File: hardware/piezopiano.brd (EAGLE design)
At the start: 90 x 99.8 mm, 110 parts, among them J2 CON2, Q1 DMN3404L, Q2 DMN3404L, Q3 DMN3404L, Q4 DMN3404L, Q5 DMN3404L, Q6 DMN3404L, Q7 DMN3404L, Q8 DMN3404L, Q9 DNP, U1 CH340E_MSOP10, U2 ATMEGA4809, U3 DNP

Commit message: Reverted to local libraries
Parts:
- DEBUG: value AVR-UPDI-6-SKEDD -> DNP
- JP1, JP2, JP3, JP4, JP5, JP6: value PINROW-1X5 -> DNP

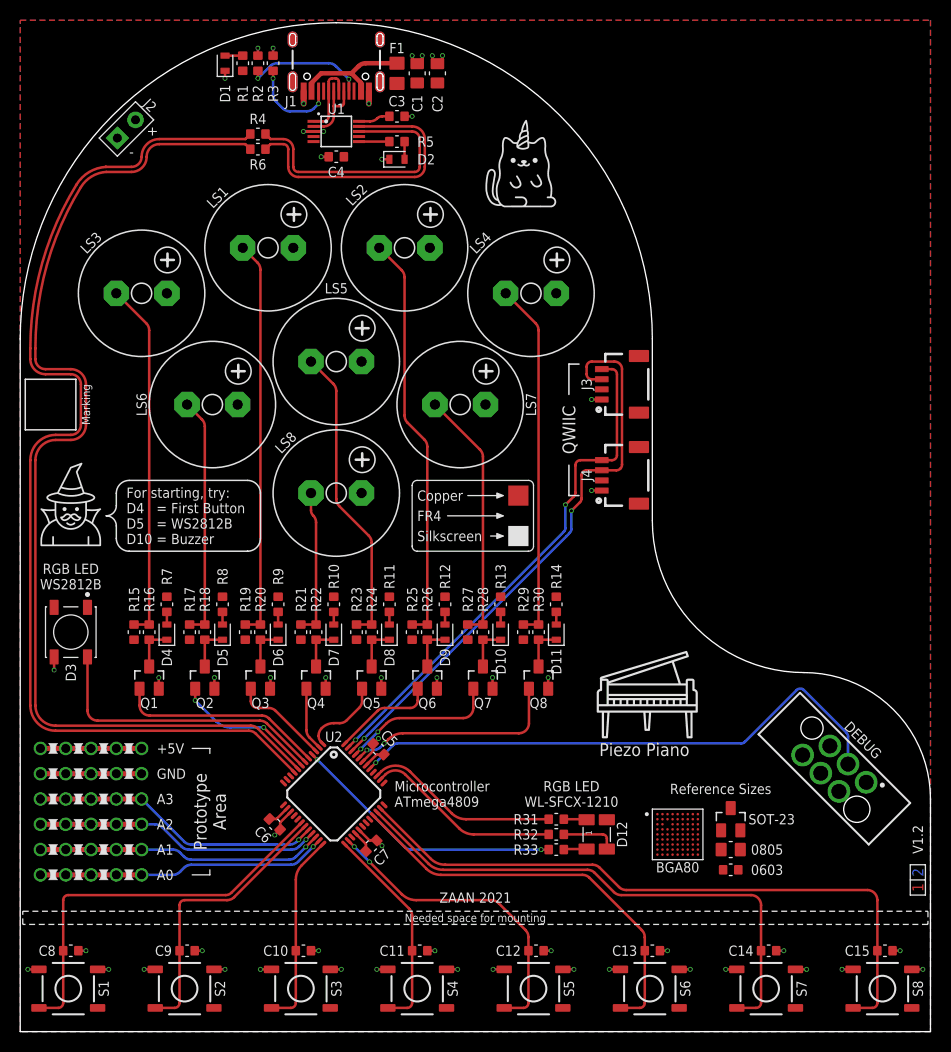
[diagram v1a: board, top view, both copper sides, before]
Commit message: Fixed silkscreen errors
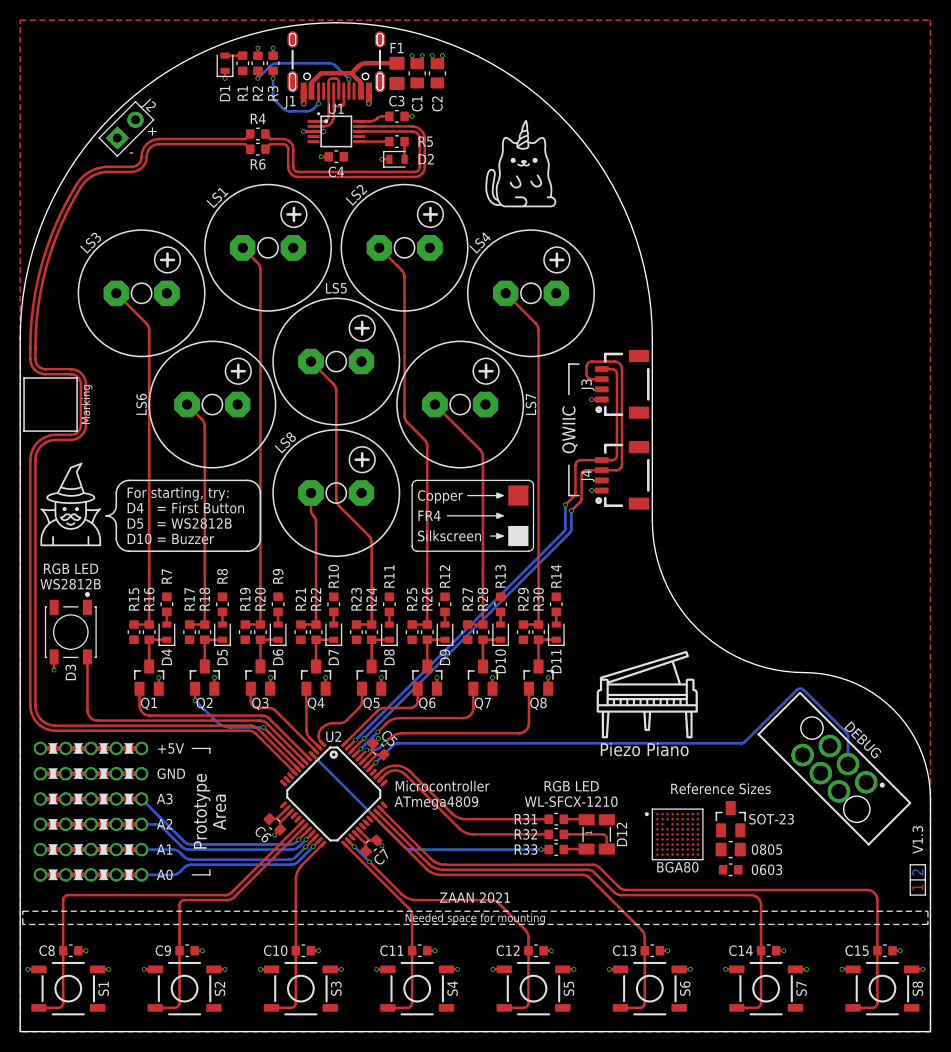
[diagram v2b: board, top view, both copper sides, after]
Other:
- board text added: "V1.3"
- board text removed: "V1.2"
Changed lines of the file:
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@@
 <drawing>
 <settings>
-<setting alwaysvectorfont="no"/>
+<setting alwaysvectorfont="yes"/>
 <setting verticaltext="up"/>
 </settings>
@@
 <layer number="24" name="bOrigins" color="15" fill="1" visible="yes" active="yes"/>
 <layer number="25" name="tNames" color="7" fill="1" visible="yes" active="yes"/>
-<layer number="26" name="bNames" color="7" fill="1" visible="no" active="yes"/>
+<layer number="26" name="bNames" color="7" fill="1" visible="yes" active="yes"/>
 <layer number="27" name="tValues" color="7" fill="1" visible="no" active="yes"/>
 <layer number="28" name="bValues" color="7" fill="1" visible="no" active="yes"/>
@@
 ornare magna eget, malesuada nunc. Fusce malesuada massa felis, cursus finibus dui
 viverra ut. Duis commodo finibus commodo. Morbi sodales vulputate mauris, eget
-molestie ex gravida quis. Phasellus tempus velit eu orci lacinia imperdiet. Proin eget
-ipsum non lectus mattis mollis vitae id arcu. Curabitur semper tempus dignissim. Nunc
+molestie ex gravida quis. Phasellus  tempus velit eu orci lacinia imperdiet. Proin eget
+ipsum non lectus mattis mollis vitae   arcu. Curabitur semper tempus dignissim. Nunc
 efficitur magna vel nisi maximus, rhoncus laoreet leo vestibulum. Proin maximus convallis
 est ut eleifend. Etiam sollicitudin sem id congue rutrum. Integer suscipit, ante in
 consequat condimentum, est erat tempus purus, sed fringilla tortor augue sed justo.
 Ut non nisl sit amet arcu cursus commodo eget et metus.</text>
-<text x="88.75" y="19" size="1.016" layer="21" font="vector" ratio="15" rot="R90" align="center">V1.2</text>
+<text x="88.75" y="19" size="1.016" layer="21" font="vector" ratio="15" rot="R90" align="center">V1.3</text>
 <text x="57.25" y="27.25" size="1.27" layer="21" font="vector" ratio="15">Piezo Piano</text>
 <text x="10.5" y="51" size="1.016" layer="21" font="vector" ratio="15" align="center-left">For starting, try:
@@
 <via x="56.5" y="53.5" extent="1-16" drill="0.3"/>
 <contactref element="J2" pad="1"/>
-<wire x1="39.75" y1="96.5" x2="40.75" y2="96.5" width="0" layer="19" extent="1-1"/>
-<wire x1="35.57" y1="98.095" x2="38.75" y2="96.5" width="0" layer="19" extent="16-16"/>
 <wire x1="35.57" y1="98.095" x2="35.57" y2="98.095" width="0" layer="19" extent="1-16"/>
-<wire x1="35.57" y1="93.915" x2="39.25" y2="95.7" width="0" layer="19" extent="1-16"/>
 <wire x1="35.57" y1="93.915" x2="35.57" y2="93.915" width="0" layer="19" extent="1-16"/>
-<wire x1="34.475" y1="92.99" x2="35.57" y2="93.915" width="0" layer="19" extent="1-16"/>
-<wire x1="38" y1="90.5" x2="34.475" y2="91.75" width="0" layer="19" extent="1-1"/>
-<wire x1="36.5" y1="86.25" x2="38" y2="90.5" width="0" layer="19" extent="1-1"/>
-<wire x1="30" y1="89" x2="34.475" y2="91.75" width="0" layer="19" extent="1-1"/>
-<wire x1="29.75" y1="86.5" x2="30" y2="89" width="0" layer="19" extent="1-1"/>
-<wire x1="28.025" y1="91.75" x2="28" y2="89" width="0" layer="19" extent="1-1"/>
-<wire x1="26.93" y1="93.915" x2="28.025" y2="92.99" width="0" layer="19" extent="1-16"/>
+<wire x1="26.93" y1="98.095" x2="26.93" y2="98.095" width="0" layer="19" extent="1-16"/>
 <wire x1="26.93" y1="93.915" x2="26.93" y2="93.915" width="0" layer="19" extent="1-16"/>
-<wire x1="25" y1="96.5" x2="26.93" y2="93.915" width="0" layer="19" extent="1-16"/>
-<wire x1="23.5" y1="97.25" x2="25" y2="97.25" width="0" layer="19" extent="1-1"/>
-<wire x1="26.93" y1="98.095" x2="25" y2="97.25" width="0" layer="19" extent="16-16"/>
-<wire x1="26.93" y1="98.095" x2="26.93" y2="98.095" width="0" layer="19" extent="1-16"/>
-<wire x1="20.25" y1="95" x2="23.5" y2="96.5" width="0" layer="19" extent="1-1"/>
-<wire x1="9.601971875" y1="88.351971875" x2="20.25" y2="94.25" width="0" layer="19" extent="1-1"/>
-<wire x1="56.5" y1="62.5" x2="36.5" y2="86.25" width="0" layer="19" extent="1-1"/>
-<wire x1="57.5" y1="53.5" x2="57.5" y2="62.5" width="0" layer="19" extent="1-1"/>
-<wire x1="52.2" y1="35" x2="56.5" y2="53.5" width="0" layer="19" extent="1-1"/>
-<wire x1="46.7" y1="33.9" x2="52.2" y2="33.9" width="0" layer="19" extent="1-1"/>
-<wire x1="41.2" y1="33.9" x2="46.7" y2="33.9" width="0" layer="19" extent="1-1"/>
-<wire x1="35.7" y1="33.9" x2="41.2" y2="33.9" width="0" layer="19" extent="1-1"/>
-<wire x1="35.419415625" y1="28.980075" x2="35.7" y2="33.9" width="0" layer="19" extent="1-1"/>
-<wire x1="30.2" y1="33.9" x2="35.7" y2="33.9" width="0" layer="19" extent="1-1"/>
-<wire x1="24.75" y1="35" x2="30.2" y2="35" width="0" layer="19" extent="1-1"/>
-<wire x1="19.2" y1="33.9" x2="24.7" y2="33.9" width="0" layer="19" extent="1-1"/>
-<wire x1="13.7" y1="33.9" x2="19.2" y2="33.9" width="0" layer="19" extent="1-1"/>
-<wire x1="33.49255" y1="19.9467875" x2="33.846103125" y2="26.69965625" width="0" layer="19" extent="1-1"/>
-<wire x1="26.73968125" y1="21.714553125" x2="33.49255" y2="19.9467875" width="0" layer="19" extent="1-1"/>
-<wire x1="12" y1="25.5" x2="13.7" y2="33.9" width="0" layer="19" extent="1-1"/>
-<wire x1="9.5" y1="25.5" x2="12" y2="25.5" width="0" layer="19" extent="1-1"/>
-<wire x1="7" y1="25.5" x2="9.5" y2="25.5" width="0" layer="19" extent="1-1"/>
-<wire x1="4.5" y1="25.5" x2="7" y2="25.5" width="0" layer="19" extent="1-1"/>
-<wire x1="2" y1="25.5" x2="4.5" y2="25.5" width="0" layer="19" extent="1-1"/>
-<wire x1="3.35" y1="35.75" x2="4.5" y2="25.5" width="0" layer="19" extent="1-1"/>
-<wire x1="40.25" y1="8" x2="35.77296875" y2="18.373475" width="0" layer="19" extent="1-1"/>
-<wire x1="42.15" y1="6.155" x2="41" y2="8" width="0" layer="19" extent="1-1"/>
-<wire x1="46.75" y1="6.155" x2="43.25" y2="6.155" width="0" layer="19" extent="1-1"/>
-<wire x1="51.75" y1="8" x2="47.85" y2="6.155" width="0" layer="19" extent="1-1"/>
-<wire x1="53.65" y1="6.155" x2="52.5" y2="8" width="0" layer="19" extent="1-1"/>
-<wire x1="58.25" y1="6.155" x2="54.75" y2="6.155" width="0" layer="19" extent="1-1"/>
-<wire x1="63.25" y1="8" x2="59.35" y2="6.155" width="0" layer="19" extent="1-1"/>
-<wire x1="65.15" y1="6.155" x2="64" y2="8" width="0" layer="19" extent="1-1"/>
-<wire x1="69.75" y1="6.155" x2="66.25" y2="6.155" width="0" layer="19" extent="1-1"/>
-<wire x1="74.75" y1="8" x2="70.85" y2="6.155" width="0" layer="19" extent="1-1"/>
-<wire x1="76.65" y1="6.155" x2="75.5" y2="8" width="0" layer="19" extent="1-1"/>
-<wire x1="81.25" y1="6.155" x2="77.75" y2="6.155" width="0" layer="19" extent="1-1"/>
-<wire x1="86.25" y1="8" x2="82.35" y2="6.155" width="0" layer="19" extent="1-1"/>
-<wire x1="88.15" y1="6.155" x2="87" y2="8" width="0" layer="19" extent="1-1"/>
-<wire x1="36.35" y1="6.155" x2="40.25" y2="8" width="0" layer="19" extent="1-1"/>
-<wire x1="31.75" y1="6.155" x2="35.25" y2="6.155" width="0" layer="19" extent="1-1"/>
-<wire x1="29.5" y1="8" x2="30.65" y2="6.155" width="0" layer="19" extent="1-1"/>
-<wire x1="24.85" y1="6.155" x2="28.75" y2="8" width="0" layer="19" extent="1-1"/>
-<wire x1="20.25" y1="6.155" x2="23.75" y2="6.155" width="0" layer="19" extent="1-1"/>
-<wire x1="18" y1="8" x2="19.15" y2="6.155" width="0" layer="19" extent="1-1"/>
-<wire x1="13.35" y1="6.155" x2="17.25" y2="8" width="0" layer="19" extent="1-1"/>
-<wire x1="8.75" y1="6.155" x2="12.25" y2="6.155" width="0" layer="19" extent="1-1"/>
-<wire x1="6.5" y1="8" x2="7.65" y2="6.155" width="0" layer="19" extent="1-1"/>
-<wire x1="1.85" y1="6.155" x2="5.75" y2="8" width="0" layer="19" extent="1-1"/>
-<wire x1="80.9490125" y1="23.754934375" x2="86.25" y2="8" width="0" layer="19" extent="1-1"/>
 </signal>
 <signal name="D2">

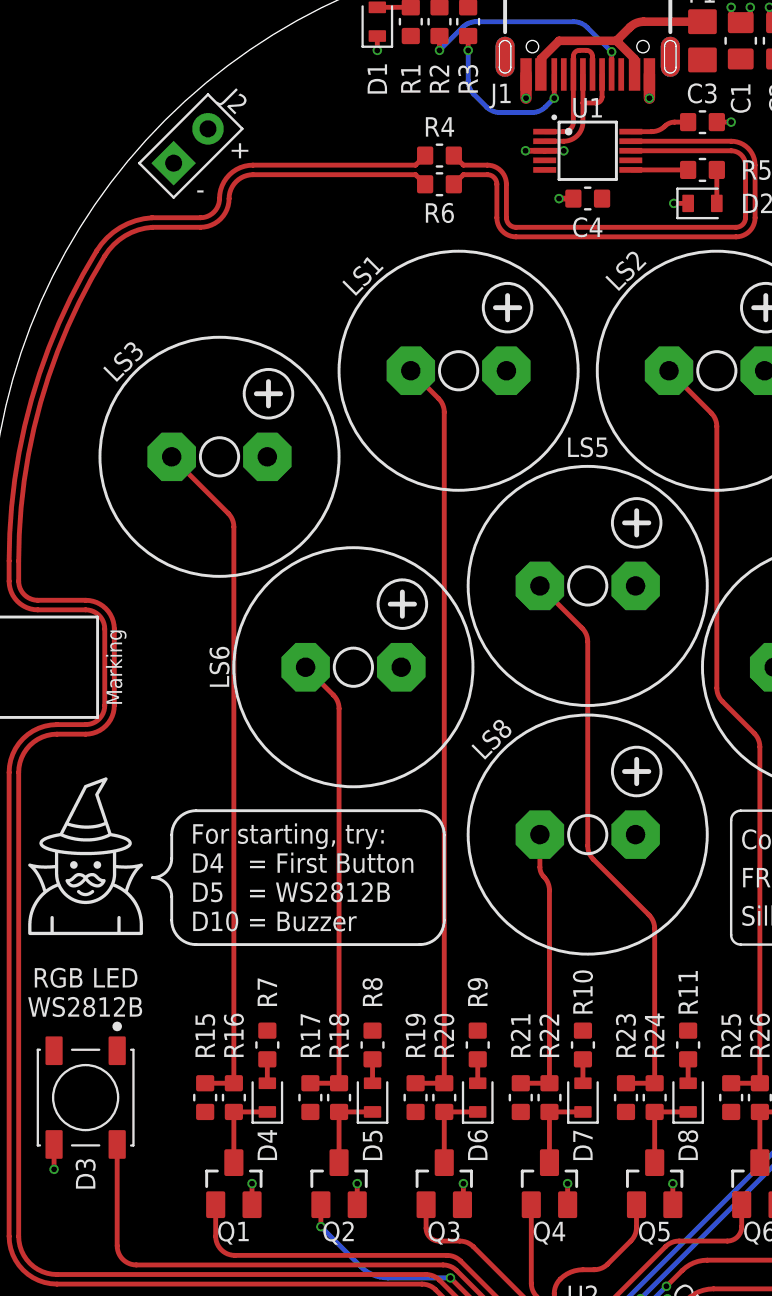
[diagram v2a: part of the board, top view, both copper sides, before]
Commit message: Added UART RST
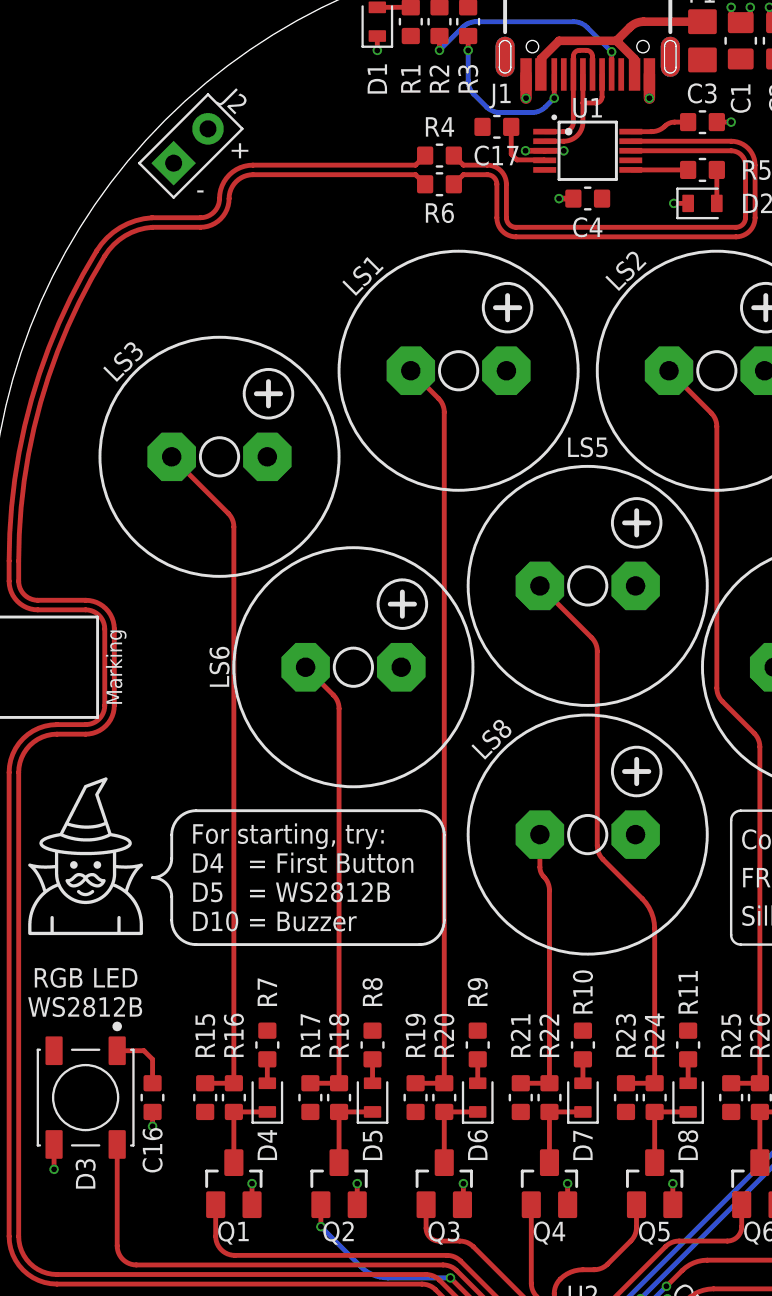
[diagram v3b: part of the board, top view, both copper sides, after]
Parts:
- added C16, C17: 100n, zaan-Capacitors:C0603
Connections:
- new net N$1: C17.1, U1.4
- net +5V: now also C16.1
- net GND: now also C16.2
- net RESETN: now also C17.2
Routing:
- net N$1: track 0.00 -> 3.31 mm
- net +5V: track 6.55 -> 9.83 mm
- net GND: track 57.8 -> 58.6 mm, vias 52 -> 53
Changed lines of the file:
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@@
 <layer number="24" name="bOrigins" color="15" fill="1" visible="yes" active="yes"/>
 <layer number="25" name="tNames" color="7" fill="1" visible="yes" active="yes"/>
-<layer number="26" name="bNames" color="7" fill="1" visible="yes" active="yes"/>
+<layer number="26" name="bNames" color="7" fill="1" visible="no" active="yes"/>
 <layer number="27" name="tValues" color="7" fill="1" visible="no" active="yes"/>
 <layer number="28" name="bValues" color="7" fill="1" visible="no" active="yes"/>
@@
 <element name="U$1" library="zaan-Symbol-Artwork" package="CATICORN-7MM" value="" x="46" y="81.5" smashed="yes"/>
 <element name="U$8" library="zaan-Symbol-Artwork" package="EXPLANATION-2-2MM" package3d_urn="urn:adsk.eagle:package:31668745/2" value="" x="49.25" y="51" smashed="yes" rot="R180"/>
+<element name="C16" library="zaan-Capacitors" package="C0603" package3d_urn="urn:adsk.eagle:package:16758953/4" value="100n" x="8.5" y="39.5" smashed="yes" rot="R270">
+<attribute name="DESCRIPTION" value="Chip Capacitor" x="8.5" y="39.5" size="1.778" layer="27" rot="R270" display="off"/>
+<attribute name="DIELECTRIC" value="X7R" x="8.5" y="39.5" size="1.778" layer="27" rot="R270" display="off"/>
+<attribute name="MF" value="Yageo" x="8.5" y="39.5" size="1.778" layer="27" rot="R270" display="off"/>
+<attribute name="MPN" value="CC0603JRX7R9BB104" x="8.5" y="39.5" size="1.778" layer="27" rot="R270" display="off"/>
+<attribute name="NAME" x="8.5" y="36.75" size="1.016" layer="25" font="vector" ratio="15" rot="R270" align="center"/>
+<attribute name="PACKAGE" value="1606" x="8.5" y="39.5" size="1.778" layer="27" rot="R270" display="off"/>
+<attribute name="PACKAGE-IN" value="0603" x="8.5" y="39.5" size="1.778" layer="27" rot="R270" display="off"/>
+<attribute name="TOLERANCE" value="5%" x="8.5" y="39.5" size="1.778" layer="27" rot="R270" display="off"/>
+<attribute name="VALUE" x="7" y="39.5" size="1.016" layer="27" font="vector" ratio="15" rot="R270" align="center"/>
+<attribute name="VOLTAGE" value="50V" x="8.5" y="39.5" size="1.778" layer="27" rot="R270" display="off"/>
+</element>
+<element name="C17" library="zaan-Capacitors" package="C0603" package3d_urn="urn:adsk.eagle:package:16758953/4" value="100n" x="26.5" y="90.25" smashed="yes" rot="R180">
+<attribute name="DESCRIPTION" value="Chip Capacitor" x="26.5" y="90.25" size="1.778" layer="27" font="vector" ratio="15" rot="R180" display="off"/>
+<attribute name="DIELECTRIC" value="X7R" x="26.5" y="90.25" size="1.778" layer="27" font="vector" ratio="15" rot="R180" display="off"/>
+<attribute name="MF" value="Yageo" x="26.5" y="90.25" size="1.778" layer="27" font="vector" ratio="15" rot="R180" display="off"/>
+<attribute name="MPN" value="CC0603JRX7R9BB104" x="26.5" y="90.25" size="1.778" layer="27" font="vector" ratio="15" rot="R180" display="off"/>
+<attribute name="NAME" x="26.5" y="88.75" size="1.016" layer="25" font="vector" ratio="15" rot="R180" align="center"/>
+<attribute name="PACKAGE" value="1606" x="26.5" y="90.25" size="1.778" layer="27" font="vector" ratio="15" rot="R180" display="off"/>
+<attribute name="PACKAGE-IN" value="0603" x="26.5" y="90.25" size="1.778" layer="27" font="vector" ratio="15" rot="R180" display="off"/>
+<attribute name="TOLERANCE" value="5%" x="26.5" y="90.25" size="1.778" layer="27" font="vector" ratio="15" rot="R180" display="off"/>
+<attribute name="VALUE" x="26.5" y="91.75" size="1.016" layer="27" font="vector" ratio="15" rot="R180" align="center"/>
+<attribute name="VOLTAGE" value="50V" x="26.5" y="90.25" size="1.778" layer="27" font="vector" ratio="15" rot="R180" display="off"/>
+</element>
 </elements>
 <signals>
@@
 <via x="56.5" y="53.5" extent="1-16" drill="0.3"/>
 <contactref element="J2" pad="1"/>
+<contactref element="C16" pad="2"/>
+<wire x1="8.5" y1="38.75" x2="8.5" y2="38" width="0.254" layer="1"/>
+<via x="8.5" y="38" extent="1-16" drill="0.3"/>
 <wire x1="35.57" y1="98.095" x2="35.57" y2="98.095" width="0" layer="19" extent="1-16"/>
 <wire x1="35.57" y1="93.915" x2="35.57" y2="93.915" width="0" layer="19" extent="1-16"/>
@@
 <contactref element="D12" pad="4"/>
 <contactref element="J2" pad="2"/>
+<contactref element="C16" pad="1"/>
+<wire x1="6.65" y1="41.95" x2="8.05" y2="41.95" width="0.254" layer="1"/>
+<wire x1="8.05" y1="41.95" x2="8.5" y2="41.5" width="0.254" layer="1"/>
+<wire x1="8.5" y1="41.5" x2="8.5" y2="40.25" width="0.254" layer="1"/>
 </signal>
 <signal name="N$2">
@@
 <wire x1="33.25" y1="40.25" x2="34.75" y2="40.25" width="0.254" layer="1"/>
 <wire x1="34.75" y1="40.25" x2="34.75" y2="48.3357875" width="0.254" layer="1"/>
-<wire x1="34.75" y1="48.3357875" x2="34.45710625" y2="49.04289375" width="0.254" layer="1" curve="45"/>
-<wire x1="34.45710625" y1="49.04289375" x2="31.54289375" y2="51.95710625" width="0.254" layer="1"/>
-<wire x1="31.54289375" y1="51.95710625" x2="31.25" y2="52.6642125" width="0.254" layer="1" curve="-45"/>
-<wire x1="31.25" y1="52.6642125" x2="31.25" y2="63.3357875" width="0.254" layer="1"/>
-<wire x1="31.25" y1="63.3357875" x2="30.95710625" y2="64.04289375" width="0.254" layer="1" curve="45"/>
-<wire x1="30.95710625" y1="64.04289375" x2="28.75" y2="66.25" width="0.254" layer="1"/>
+<wire x1="34.75" y1="48.3357875" x2="34.10355" y2="49.89645" width="0.254" layer="1" curve="45"/>
+<wire x1="34.10355" y1="49.89645" x2="32.04289375" y2="51.95710625" width="0.254" layer="1"/>
+<wire x1="32.04289375" y1="51.95710625" x2="31.75" y2="52.6642125" width="0.254" layer="1" curve="-45"/>
+<wire x1="31.75" y1="52.6642125" x2="31.75" y2="62.8357875" width="0.254" layer="1"/>
+<wire x1="31.75" y1="62.8357875" x2="31.45710625" y2="63.54289375" width="0.254" layer="1" curve="45"/>
+<wire x1="31.45710625" y1="63.54289375" x2="28.75" y2="66.25" width="0.254" layer="1"/>
 </signal>
 <signal name="N$6">
@@
 <signal name="RESETN">
 <contactref element="U2" pad="40"/>
+<contactref element="C17" pad="2"/>
+<wire x1="34.9067625" y1="25.638996875" x2="25.75" y2="90.25" width="0" layer="19" extent="1-1"/>
 </signal>
 <signal name="D3~">
@@
 <wire x1="57.5857875" y1="19.5" x2="53.75" y2="19.5" width="0.254" layer="1"/>
 </signal>
+<signal name="N$1">
+<contactref element="U1" pad="4"/>
+<contactref element="C17" pad="1"/>
+<wire x1="29" y1="88.5" x2="28.977" y2="88.523" width="0.254" layer="1"/>
+<wire x1="28.977" y1="88.523" x2="27.55241875" y2="88.523" width="0.254" layer="1"/>
+<wire x1="27.55241875" y1="88.523" x2="27.25" y2="88.82541875" width="0.254" layer="1"/>
+<wire x1="27.25" y1="88.82541875" x2="27.25" y2="90.25" width="0.254" layer="1"/>
+</signal>
 </signals>
